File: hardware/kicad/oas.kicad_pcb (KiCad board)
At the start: 2 copper layers, 120 x 103.5 mm, 69 parts, among them J1 Phoenix_MSTBA_2,5/3-G-5,08 (2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, J10 Native-USB recovery (DNP), J2 UART/Boot Recovery (DNP), J3 JST SM06B-GHS-TB (SEN66 conne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, J4 1x5 P1.27mm header (HLK-LD241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, J5 ESP32 row A (pins 1..15, ante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, J6 ESP32 row B (pins 16..30, USB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, J7 MIKROE mikroBUS pins 1..8 (AN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, J8 MIKROE mikroBUS pins 9..16 (P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, J9 JST SM04B-SRSS-TB (Qwiic / St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, Q1 AO3401A, SW1 C&K PTS645VK392LFS, U1 LM2596S-5.0, U2 TPS62933

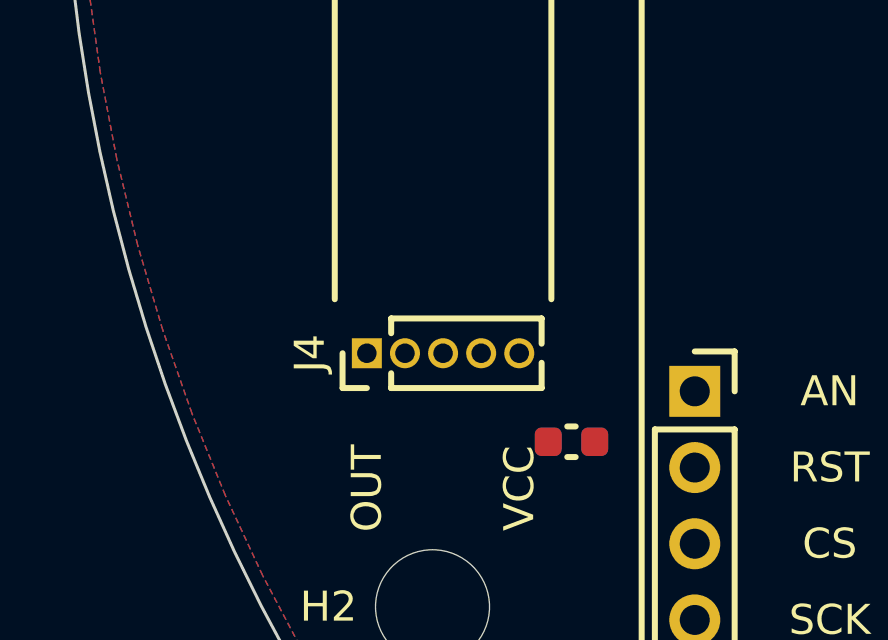
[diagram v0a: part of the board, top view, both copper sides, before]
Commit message: fix(dfm): move C11 clear of the J4 THT pads + jlcdfm --pcb-only flag
C11 (LD2410 +5V decoupling) relocated to the 11-o'clock of J4's west
end — vertical, in open copper just west of the LD2410 body shadow
(LDR1, X>=97.4 mm, which carries no courtyard). Both pads are now
3.66 / 4.99 mm from the nearest J4 THT pad — clear of the JLCPCB DFM
"tht to smd" >3.05 mm (Good) threshold. The earlier J4-south pocket
(J4 / J7 / H2 mounting hole / J4 pin-label row) could not give Good +
DRC-clean simultaneously; this open-copper spot does.

tools/jlcdfm_upload.py gains --pcb-only: runs the PCB DFM check and
stops, skipping the SMT DFM stage (no BOM / CPL upload, no BOM match).

30/30 build PASS, DRC 0 violations.

Co-Authored-By: Claude Opus 4.7 <noreply@anthropic.com>
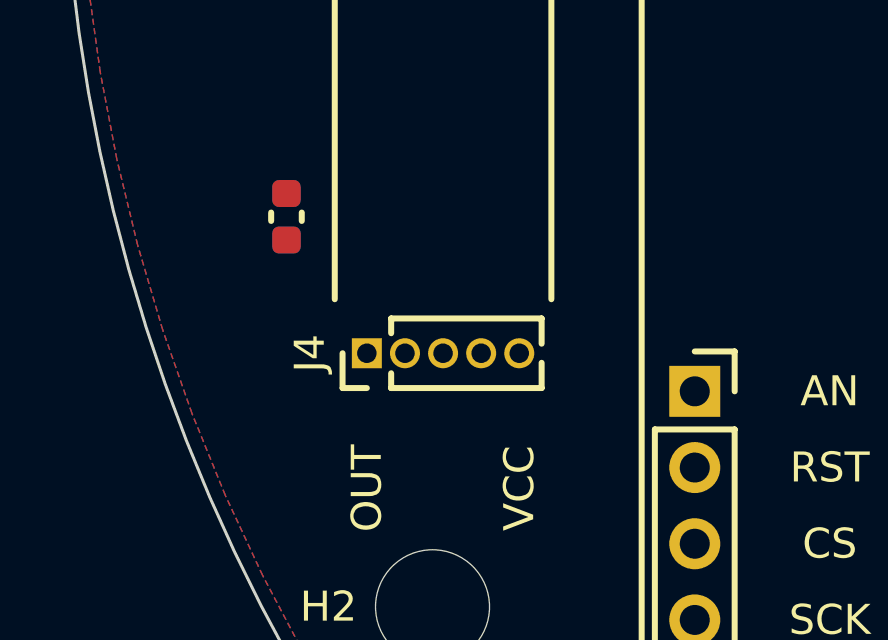
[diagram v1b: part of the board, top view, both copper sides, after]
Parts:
- moved C11 12.1 mm to (96.0, 119.5), turned to 270 degrees
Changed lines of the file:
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@@
 (footprint "Capacitor_SMD:C_0603_1608Metric"
 	(layer "F.Cu")
-	(at 105.5 127 0)
+	(at 96 119.5 270)
 (property "Reference" "C11"
-	(at 0 -1.45 0)
+	(at 0 -1.45 270)
 	(layer "F.SilkS")
 			(hide yes)
@@
 )
 (property "Value" "100nF"
-	(at 0 1.45 0)
+	(at 0 1.45 270)
 	(layer "F.Fab")
 			(hide yes)
@@
 	(effects (font (size 1.27 1.27)))
 )
-(property "Description" "100 nF local decoupling for LD2410 (J4 pin 5 / +5V). Stays ~2.1 mm (Warning) from the J4 / J7 THT pads — the pocket (J4 N / J7 E / H2 mounting-hole SW / J4 pin-label row) is geometrically too tight for full clearance, and JLCPCB DFM 'tht to smd' Warning is a solder-wicking caution, not a defect."
+(property "Description" "100 nF local decoupling for LD2410 (J4 pin 5 / +5V). v0.44: vertical, placed at the 11-o'clock of J4's west end — west of the LD2410 body (LDR1, X>=97.4) in open copper. Every pad >3.6 mm (Good) from the J4 THT pad row — clears the JLCPCB DFM 'tht to smd' >3.05 mm rule."
 	(at 0 0 0)
 	(layer "F.Fab")
@@
 		)
 	(pad "1" smd roundrect
-			(at -0.775 0)
+			(at -0.775 0 270)
 			(size 0.9 0.95)
 			(layers "F.Cu" "F.Mask" "F.Paste")
@@
 		)
 	(pad "2" smd roundrect
-			(at 0.775 0)
+			(at 0.775 0 270)
 			(size 0.9 0.95)
 			(layers "F.Cu" "F.Mask" "F.Paste")
@@
 )
 (gr_text "C11"
-	(at 105.5 125 0)
-	(layer "F.Fab")
-	(effects
+	(at 96 117.5 0)
+	(layer "F.Fab")
+	(effects

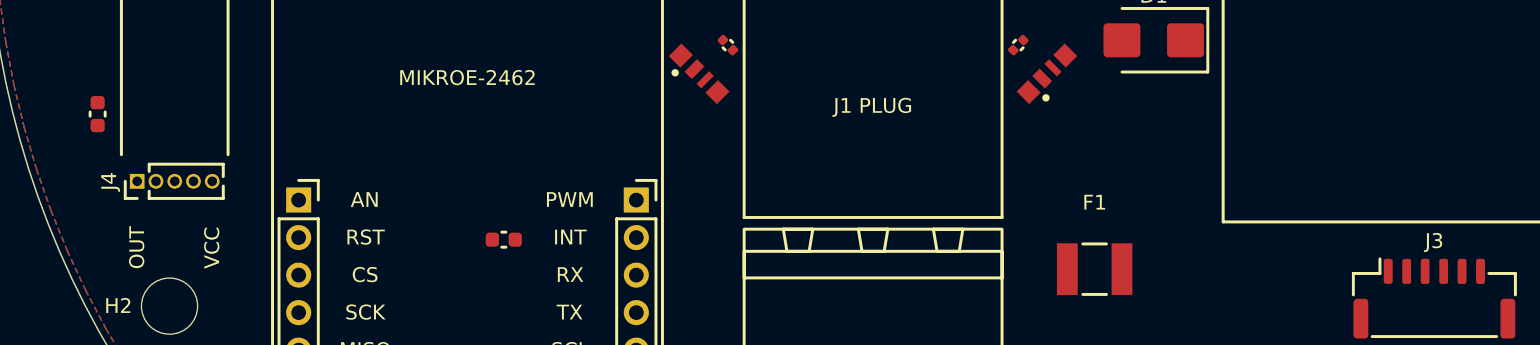
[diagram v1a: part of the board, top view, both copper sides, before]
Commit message: fix(dfm): clear the 4 remaining JLCDFM PCB warning buckets (v0.45)
JLCDFM PCB DFM stood at 0 Danger / 64 Warning (commit 93403da). All four
warning categories addressed:

1. tht to smd (1 W @ 2.98 mm) — C11 (LD2410 decoupling) sat 2.98 mm from
   the nearest J4 THT pad, 0.07 mm short of the >3.05 mm rule. Nudged C11
   0.5 mm north (Y +14.5 -> +14.0) into the open field NW of J4 (no
   neighbour within 4 mm); nearest J4 pad now ~3.4 mm. COMPONENT_ANCHORS
   kept in lock-step.

2. Solder mask opening exposing trace (20 W @ 0.14-0.15 mm) — the stage-20
   export copy widens every THT pad solder-mask opening by 0.05 mm; at the
   0.20 mm GND-pour pad clearance that left only a 0.15 mm mask web to the
   pour. Raised gnd_zone() connect_pads clearance 0.20 -> 0.30 mm => 0.25 mm
   web. GND-net pads unaffected (they connect via thermal reliefs).

3. Silkscreen to pad (40 W @ 0.16-0.17 mm) — the v0.44 silk-width lift
   (0.20 mm strokes) pushed silk edges ~0.04 mm closer to pads; the old
   0.15 mm export-copy strip threshold left 0.16-0.17 mm survivors. Raised
   SILK_PAD_MIN_CLEARANCE_MM 0.15 -> 0.22 mm.

4. Silkscreen line width (3 W @ 0.15 mm) — _lift_silk_line_widths lifted
   fp_text / gr_text strokes but not footprint (property "Reference" ...)
   blocks, so 3 visible designators plotted at 0.15 mm. Added "property" to
   SILK_DRAWING_KINDS; made the block parser string-aware so parens inside
   a quoted property value cannot perturb the depth count.

build.py 30/30 PASS (DRC 0, ERC 0, determinism OK).

Co-Authored-By: Claude Opus 4.7 <noreply@anthropic.com>
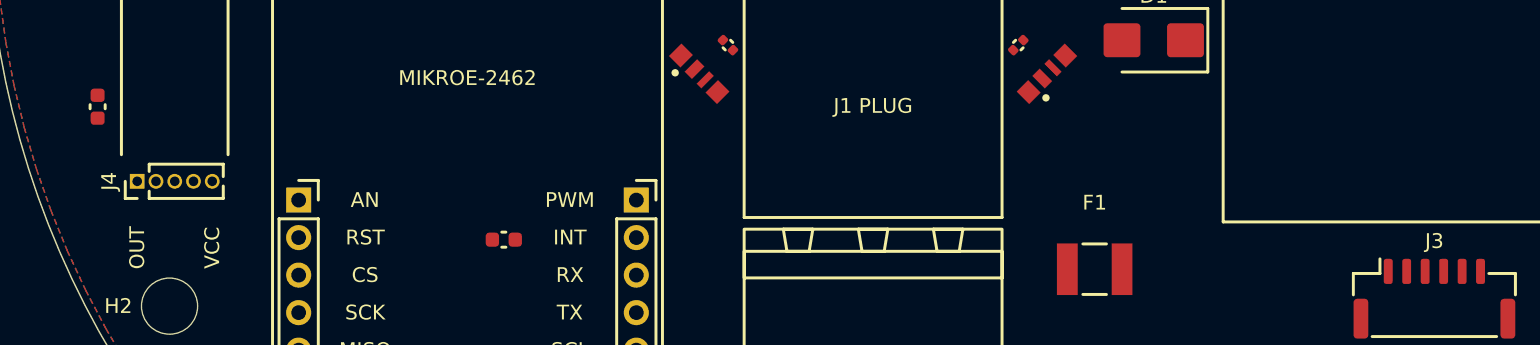
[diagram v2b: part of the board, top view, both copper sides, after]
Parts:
- moved C11 0.50 mm to (96.0, 119.0)

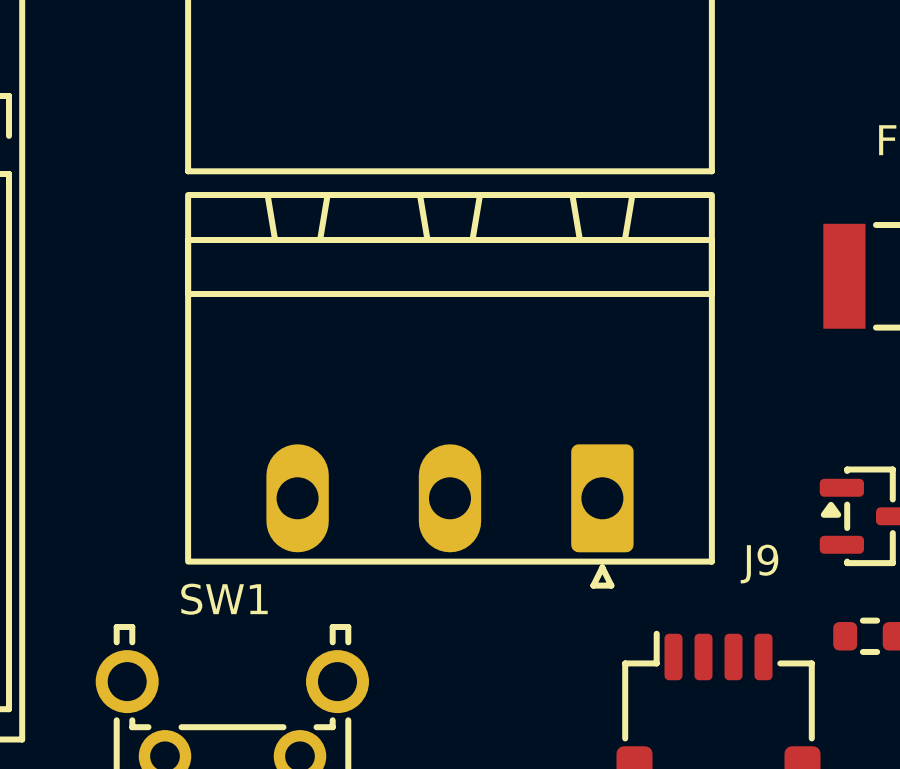
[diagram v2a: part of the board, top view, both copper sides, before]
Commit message: fix(dfm): resolve the last 2 JLCDFM PCB warnings — J1<->J9 + silk fp_poly
Follow-up to 7ea05c1. The first pass cleared mask-exposing-trace (20->0)
and silk-line-width (3->0); a JLCDFM re-measure left 0 Danger / 6 Warning:

tht to smd (1 W @ 2.98 mm) — 7ea05c1 mis-targeted this as C11 (the
pre-compact note assumed "a 0603 under the ESP32"). The flagged SMD pad is
rect 0.6x1.55 mm, a JST-SH pad: the real pair is J9.1 (Qwiic SMD) <-> J1.1
(easternmost 24 V terminal-block THT pad), 2.98 mm diagonal. Moving J9
east ran its body courtyard into R1 (DRC courtyards_overlap). Fixed
instead by nudging J1 0.4 mm north (J1_PCB_Y +32.4 -> +32.0) — J1 has
7.8 mm of open space north (nearest LED D12), so the move is
unconstrained. J1.1<->J9.1 now 3.28 mm AABB (~3.33 mm JLCDFM). The
v0.45-C11 nudge from 7ea05c1 is kept — harmless and still valid.

Silkscreen to pad (5 W @ 0.16-0.17 mm) — the survivors are the U1 / U2 / Q1
stock pin-1 marker polygons (fp_poly), which strip_silk_near_pads kept "by
design". A pin-1 wedge 0.16-0.20 mm from its own pad gets trimmed by the
fab anyway, so strip_silk_near_pads now also strips fp_poly within the
clearance (export copy only; F.Fab pin-1 markers are untouched). Export
silk-strip count 423 -> 426.

build.py 30/30 PASS (DRC 0, ERC 0, determinism OK).

Co-Authored-By: Claude Opus 4.7 <noreply@anthropic.com>
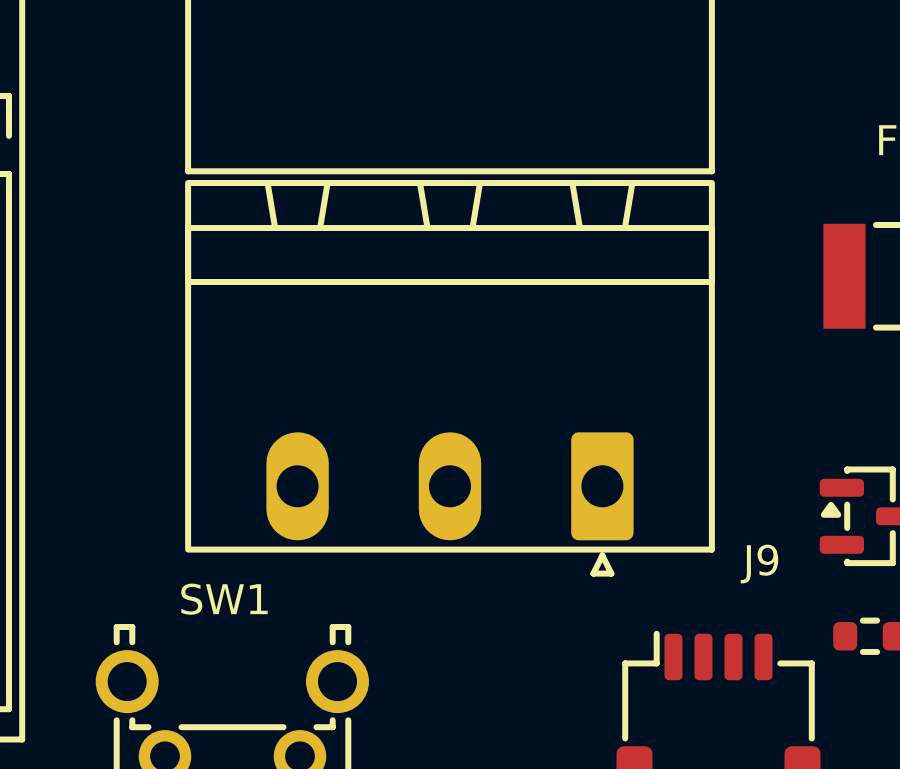
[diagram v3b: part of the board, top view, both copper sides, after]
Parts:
- moved J1 0.40 mm to (153.6, 137.0)
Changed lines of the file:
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@@
 (footprint "Connector_Phoenix_MSTB:PhoenixContact_MSTBA_2,5_3-G-5,08_1x03_P5.08mm_Horizontal"
 	(layer "F.Cu")
-	(at 153.58 137.4 180)
+	(at 153.58 137 180)
 (property "Reference" "J1"
 	(at 5.08 -3.2 180)
@@
 )
 (gr_text "J1 (24V)"
-	(at 163.5 137.4 0)
+	(at 163.5 137 0)
 	(layer "F.Fab")
 	(effects
@@
 )
 (gr_text "24V"
-	(at 153.58 136.6 0)
+	(at 153.58 136.2 0)
 	(layer "F.Fab")
 	(effects
@@
 )
 (gr_text "GND"
-	(at 148.5 136.6 0)
+	(at 148.5 136.2 0)
 	(layer "F.Fab")
 	(effects
@@
 )
 (gr_text "PE"
-	(at 143.42 136.6 0)
+	(at 143.42 136.2 0)
 	(layer "F.Fab")
 	(effects
